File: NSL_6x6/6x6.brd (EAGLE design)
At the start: 38.1 x 38.1 mm, 73 parts, among them IC1 _, Q1 BC857AT115, Q2 BC857AT115, Q3 BC857AT115, Q4 BC857AT115, Q5 BC857AT115, Q6 BC857AT115, Q7 FMB2222A, Q8 FMB2222A, Q9 FMB2222A

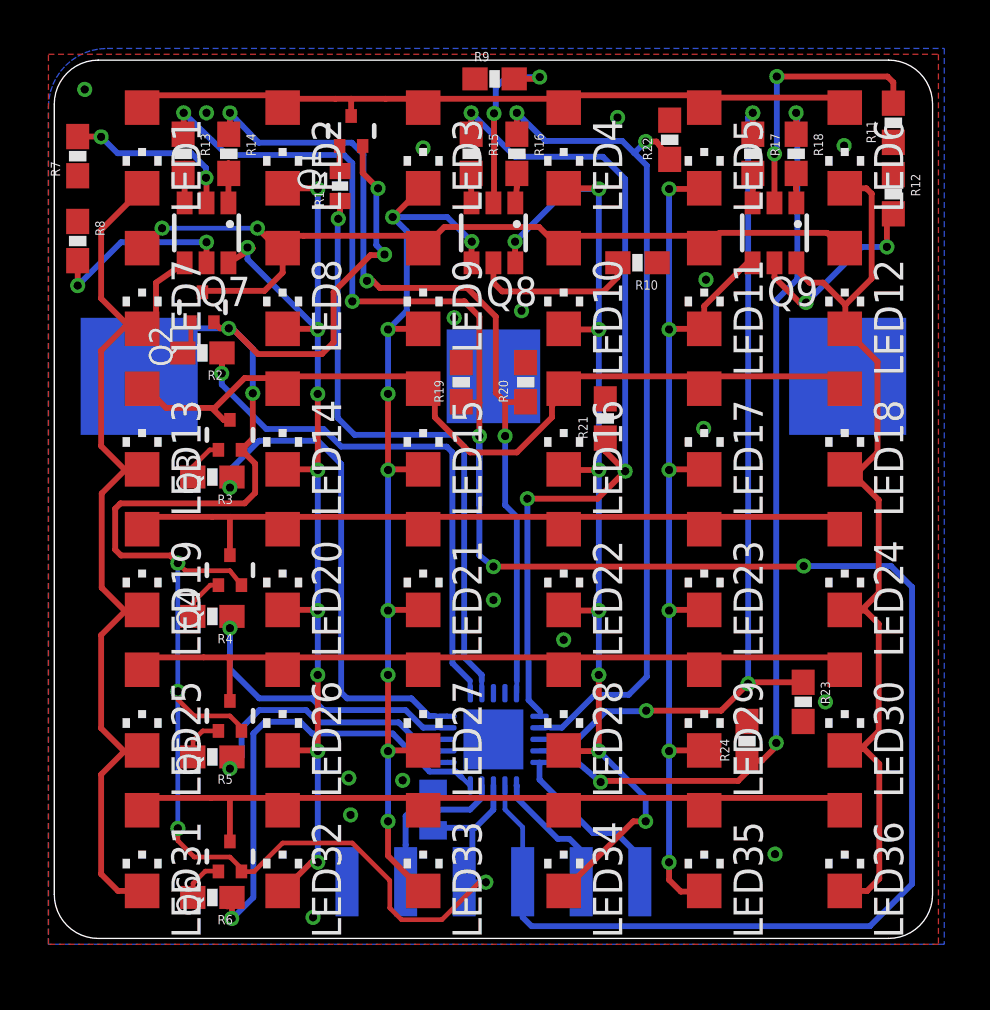
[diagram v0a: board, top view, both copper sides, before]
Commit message: 
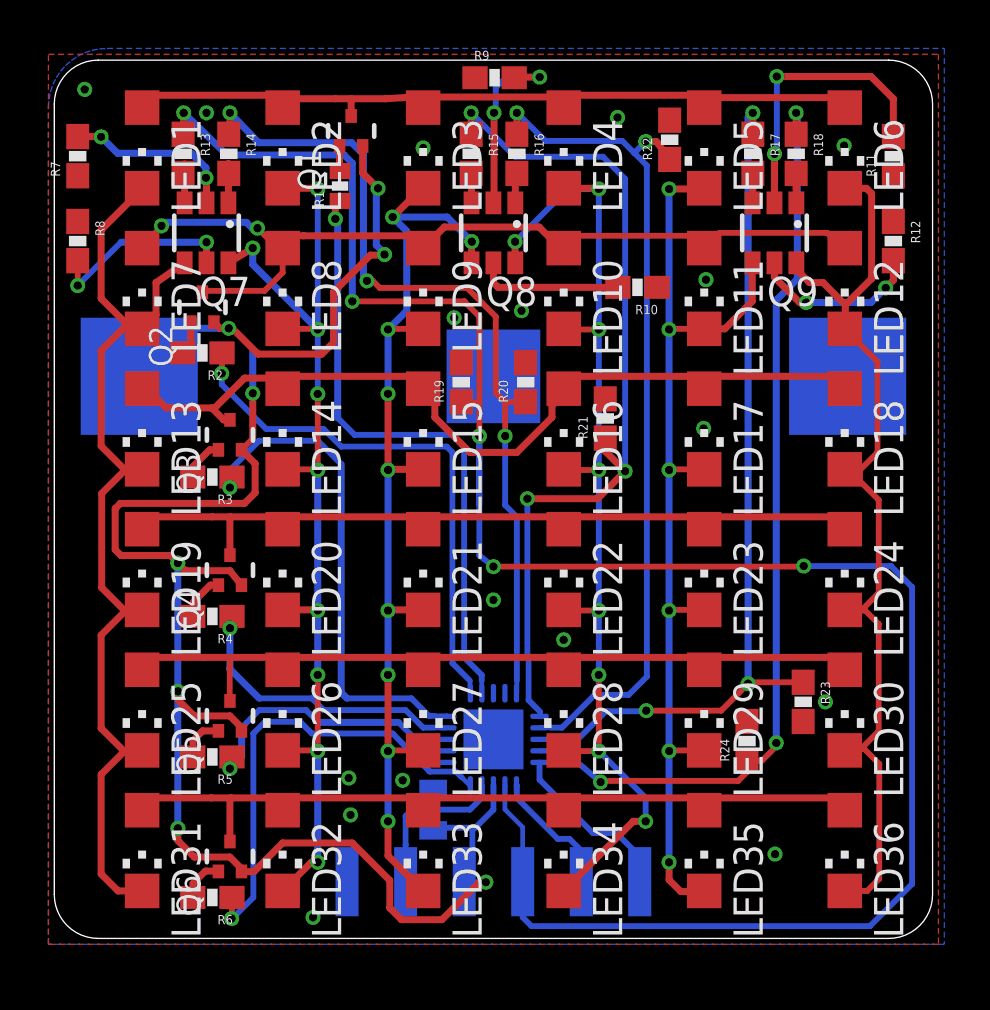
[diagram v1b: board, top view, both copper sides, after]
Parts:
- C1: value (none) -> 0.1uF
- moved R12 2.03 mm to (17.3, 11.2)
- moved R11 1.45 mm to (17.3, 14.9)
- moved R10 1.07 mm to (6.25, 9.19)
- moved R9 0.05 mm to (0.05, 18.3)
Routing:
- net N$12: track 11.6 -> 12.6 mm
- net N$11: track 8.51 -> 7.49 mm
- net N$13: track 7.29 -> 6.34 mm
- net N$8: track 43.6 -> 44.1 mm

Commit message: 
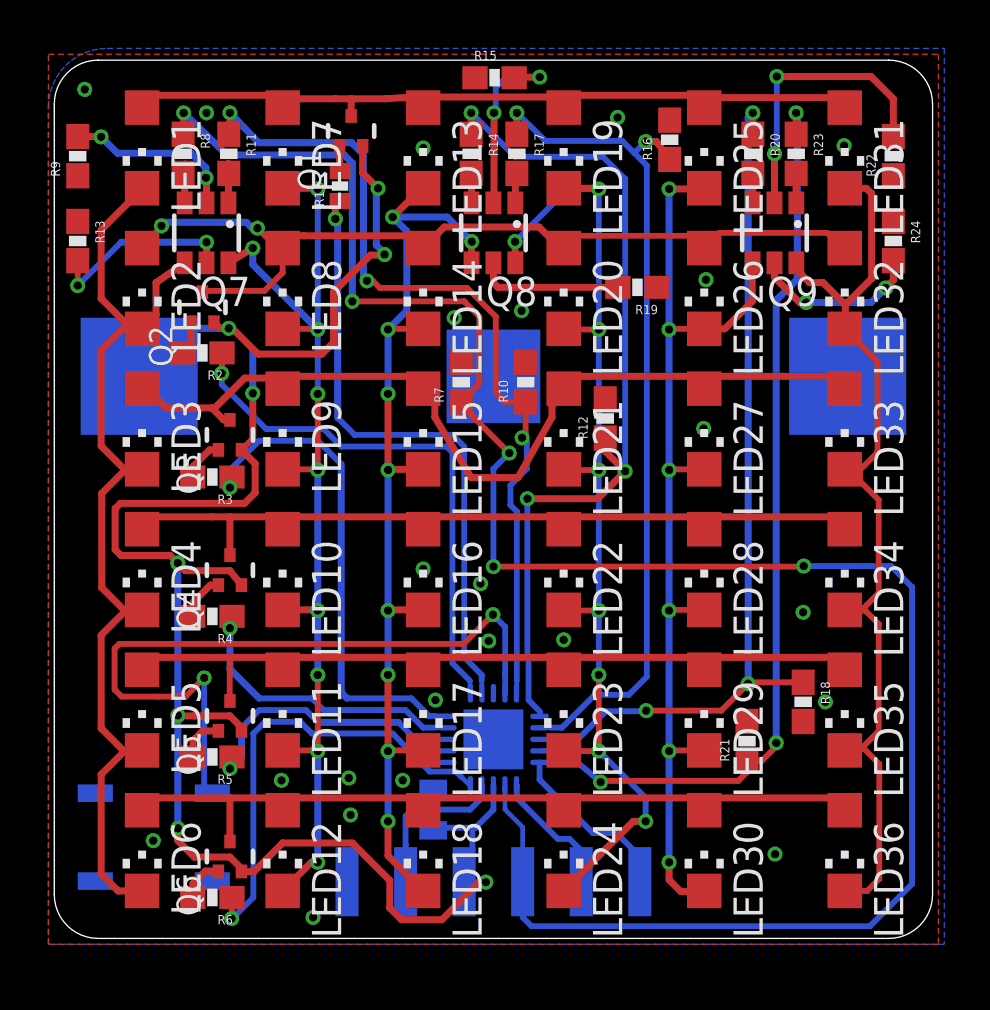
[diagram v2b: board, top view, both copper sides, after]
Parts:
- added S1: (no value), SparkFun:TACTILE_SWITCH_SMD
- R10, R12, R7: value 1K -> 10k
- R11, R8: value 1K -> 620
- R13, R15: value 620 -> 1K
- R16, R18: value 620 -> 10k
- R19, R22, R24: value 10k -> 1K
- R20, R23: value 10k -> 620
- moved LED31 43.1 mm to (15.2, 15.2)
- moved LED6 43.1 mm to (-15.2, -15.2)
- moved LED12 34.5 mm to (-9.14, -15.2)
- moved LED25 34.5 mm to (9.14, 15.2)
- moved LED32 34.5 mm to (15.2, 9.14)
- moved LED5 34.5 mm to (-15.2, -9.14)
- moved R11 28.8 mm to (-11.5, 15.0), turned to 270 degrees
- moved LED11 25.9 mm to (-9.14, -9.14)
- moved LED18 25.9 mm to (-3.05, -15.2)
- moved LED19 25.9 mm to (3.05, 15.2)
- moved LED26 25.9 mm to (9.14, 9.14)
- moved LED33 25.9 mm to (15.2, 3.05)
- moved LED4 25.9 mm to (-15.2, -3.05)
- moved R18 23.8 mm to (13.4, -8.79)
- moved R23 23.8 mm to (13.1, 15.0)
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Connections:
- new net PD6: IC1.P$9, S1.4
- net COL1_: now also R8.2; no longer R13.2
- net COL2: now also R10.1, R11.1; no longer R14.1, R20.1
- net COL2_: now also R11.2; no longer R14.2
- net COL3: now also R12.1, R14.1; no longer R15.1, R21.1
- net COL3_: now also R14.2; no longer R15.2
- net COL4: now also R17.1; no longer R22.1
- net COL4_: now also R17.2; no longer R16.2
- net COL5: now also R18.1, R20.1; no longer R17.1, R23.1
- net COL5_: now also R20.2; no longer R17.2
- net COL6: now also R21.1, R23.1; no longer R18.1, R24.1
- net COL6_: now also R23.2; no longer R18.2
- net GND: now also R10.2, R12.2, R13.1, R15.1, R16.2, R18.2, R19.1, R22.1, R24.1, R7.2, S1.1, S1.2; no longer R10.1, R11.1, R12.1, R19.2, R20.2, R22.2, R23.2, R24.2, R7.1, R8.1
- net LINE1: now also LED13.A, LED19.A, LED25.A, LED31.A, LED7.A; no longer LED2.A, LED3.A, LED4.A, LED5.A, LED6.A
- net LINE2: now also LED14.A, LED2.A, LED20.A, LED26.A, LED32.A; no longer LED10.A, LED11.A, LED12.A, LED7.A, LED9.A
- net LINE3: now also LED21.A, LED27.A, LED3.A, LED33.A, LED9.A; no longer LED13.A, LED14.A, LED16.A, LED17.A, LED18.A
- net LINE4: now also LED10.A, LED16.A, LED28.A, LED34.A, LED4.A; no longer LED19.A, LED20.A, LED21.A, LED23.A, LED24.A
- net LINE5: now also LED11.A, LED17.A, LED23.A, LED35.A, LED5.A; no longer LED25.A, LED26.A, LED27.A, LED28.A, LED30.A
- net LINE6: now also LED12.A, LED18.A, LED24.A, LED30.A, LED6.A; no longer LED31.A, LED32.A, LED33.A, LED34.A, LED35.A
- net N$10: now also R9.2; no longer R7.2
- net N$11: now also R24.2; no longer R12.2
- net N$12: now also R22.2; no longer R11.2
- net N$13: now also R19.2; no longer R10.2
- net N$14: now also R15.2; no longer R9.2
- net N$15: now also R13.2; no longer R8.2
- net N$40: now also LED2.C, LED3.C, LED4.C, LED5.C, LED6.C; no longer LED13.C, LED19.C, LED25.C, LED31.C, LED7.C
- net N$41: now also LED10.C, LED11.C, LED12.C, LED7.C, LED9.C; no longer LED14.C, LED2.C, LED20.C, LED26.C, LED32.C
- net N$42: now also LED13.C, LED14.C, LED16.C, LED17.C, LED18.C; no longer LED21.C, LED27.C, LED3.C, LED33.C, LED9.C
- net N$7: now also LED19.C, LED20.C, LED21.C, LED23.C, LED24.C; no longer LED10.C, LED16.C, LED28.C, LED34.C, LED4.C
- net N$8: now also LED25.C, LED26.C, LED27.C, LED28.C, LED30.C; no longer LED11.C, LED17.C, LED23.C, LED35.C, LED5.C
- net N$9: now also LED31.C, LED32.C, LED33.C, LED34.C, LED35.C; no longer LED12.C, LED18.C, LED24.C, LED30.C, LED6.C
- net SCK/COL1: now also R7.1, R8.1; no longer R13.1, R19.1
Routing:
- net PD6: track 0.00 -> 31.9 mm, vias 0 -> 2
- net SCK/COL1: track 91.7 -> 88.9 mm
- net LINE3: track 38.6 -> 40.4 mm
- net VCC: track 84.0 -> 83.4 mm

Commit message: 
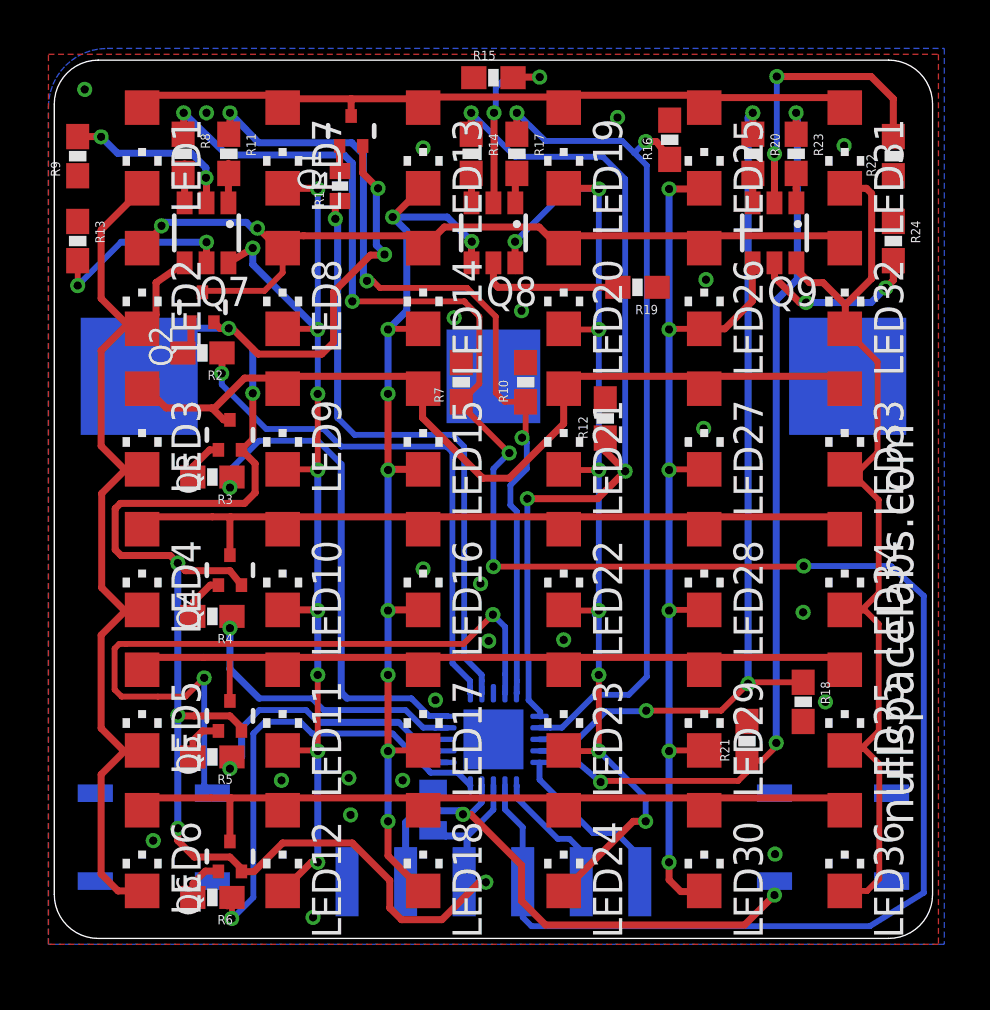
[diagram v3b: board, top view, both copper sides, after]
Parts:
- added S2: (no value), SparkFun:TACTILE_SWITCH_SMD
- moved R15 0.05 mm to (0.00, 18.3)
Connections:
- net GND: now also S2.1, S2.2
- net RST: now also S2.4
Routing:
- net RST: track 7.02 -> 24.7 mm, vias 0 -> 2
- net SCK/COL1: track 88.9 -> 89.7 mm

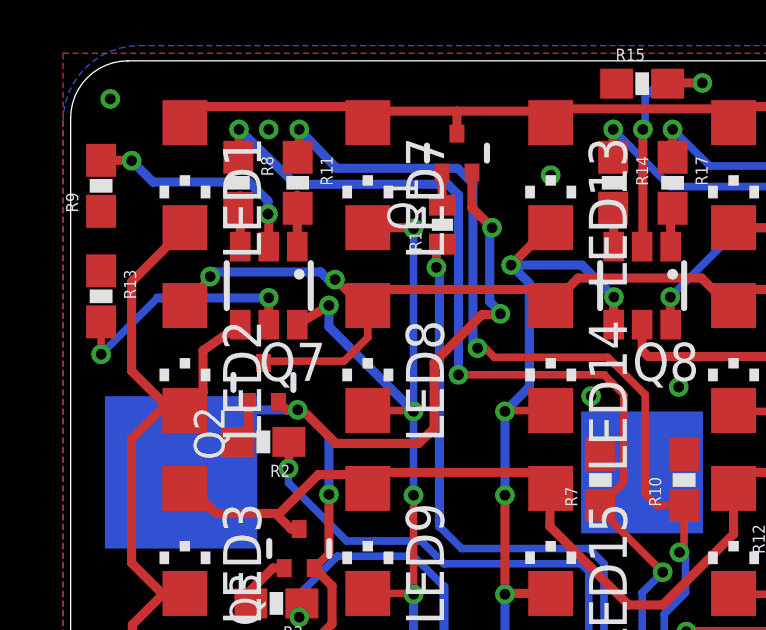
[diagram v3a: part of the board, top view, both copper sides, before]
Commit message: 
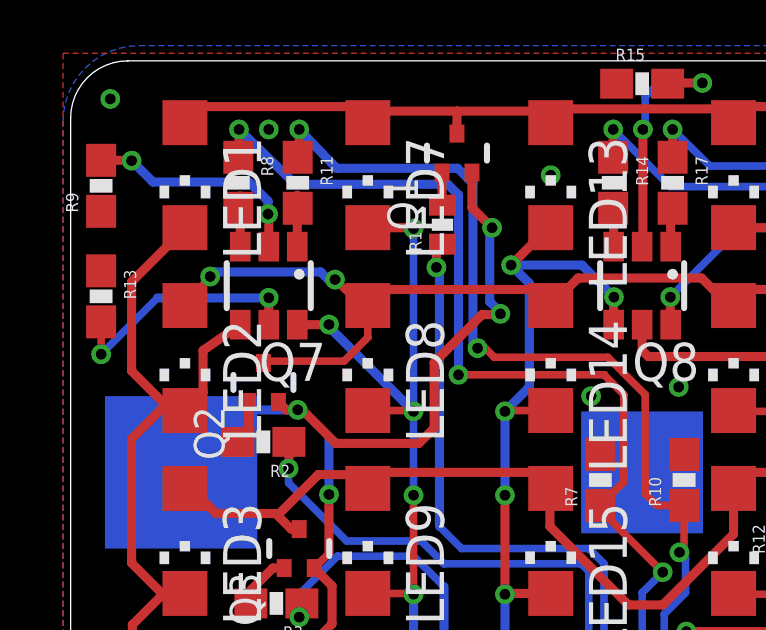
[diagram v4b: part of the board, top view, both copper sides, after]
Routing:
- net N$41: track 44.9 -> 44.0 mm
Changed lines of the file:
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@@
 <wire x1="-7.62" y1="7.366" x2="-7.648" y2="7.394" width="0.254" layer="1"/>
 <wire x1="-7.62" y1="7.366" x2="-7.62" y2="13.462" width="0.254" layer="16"/>
-<wire x1="-11.496" y1="10.257" x2="-10.444" y2="10.892" width="0.3048" layer="1"/>
-<wire x1="-10.444" y1="10.892" x2="-10.4394" y2="10.8966" width="0.254" layer="1"/>
+<wire x1="-11.496" y1="10.257" x2="-10.444" y2="10.257" width="0.3048" layer="1"/>
+<wire x1="-10.444" y1="10.257" x2="-10.4394" y2="10.2616" width="0.254" layer="1"/>
 <wire x1="-7.62" y1="-7.62" x2="-7.62" y2="-10.922" width="0.254" layer="1"/>
 <wire x1="-7.62" y1="-4.826" x2="-7.62" y2="-7.62" width="0.3048" layer="16"/>
@@
 <via x="-7.62" y="1.27" extent="1-16" drill="0.3556"/>
 <via x="-7.62" y="7.366" extent="1-16" drill="0.3556"/>
-<via x="-10.4394" y="10.8966" extent="1-16" drill="0.3556"/>
+<via x="-10.4394" y="10.2616" extent="1-16" drill="0.3556"/>
 <via x="-7.62" y="-7.62" extent="1-16" drill="0.3556"/>
 <via x="-7.62" y="4.572" extent="1-16" drill="0.3556"/>
 <wire x1="-7.62" y1="7.366" x2="-10.4394" y2="10.1854" width="0.3048" layer="16"/>
-<wire x1="-10.4394" y1="10.1854" x2="-10.4394" y2="10.8966" width="0.3048" layer="16"/>
+<wire x1="-10.4394" y1="10.1854" x2="-10.4394" y2="10.2616" width="0.3048" layer="16"/>
 </signal>
 <signal name="N$42">
